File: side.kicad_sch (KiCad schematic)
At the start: 82 parts, among them J1 Conn_01x02, J2 SWD_Connector, J3 USB_C_Receptacle_USB2.0_14P, SW1 Reset Button, SW10 SW_Push, SW11 SW_Push, SW12 SW_Push, SW13 SW_Push, SW14 SW_Push, SW15 SW_Push, SW16 SW_Push, SW17 SW_Push, SW18 SW_Push, SW19 SW_Push, SW2 SW_On_Off, SW20 SW_Push, SW21 SW_Push, SW22 SW_Push, SW23 SW_Push, SW3 SW_Push, SW4 SW_Push, SW5 SW_Push, SW6 SW_Push, SW7 SW_Push, SW8 SW_Push, SW9 SW_Push, U1 nRF52840, U2 USBLC6-2SC6, Y1 JYJE 2TJ432000NYFBC

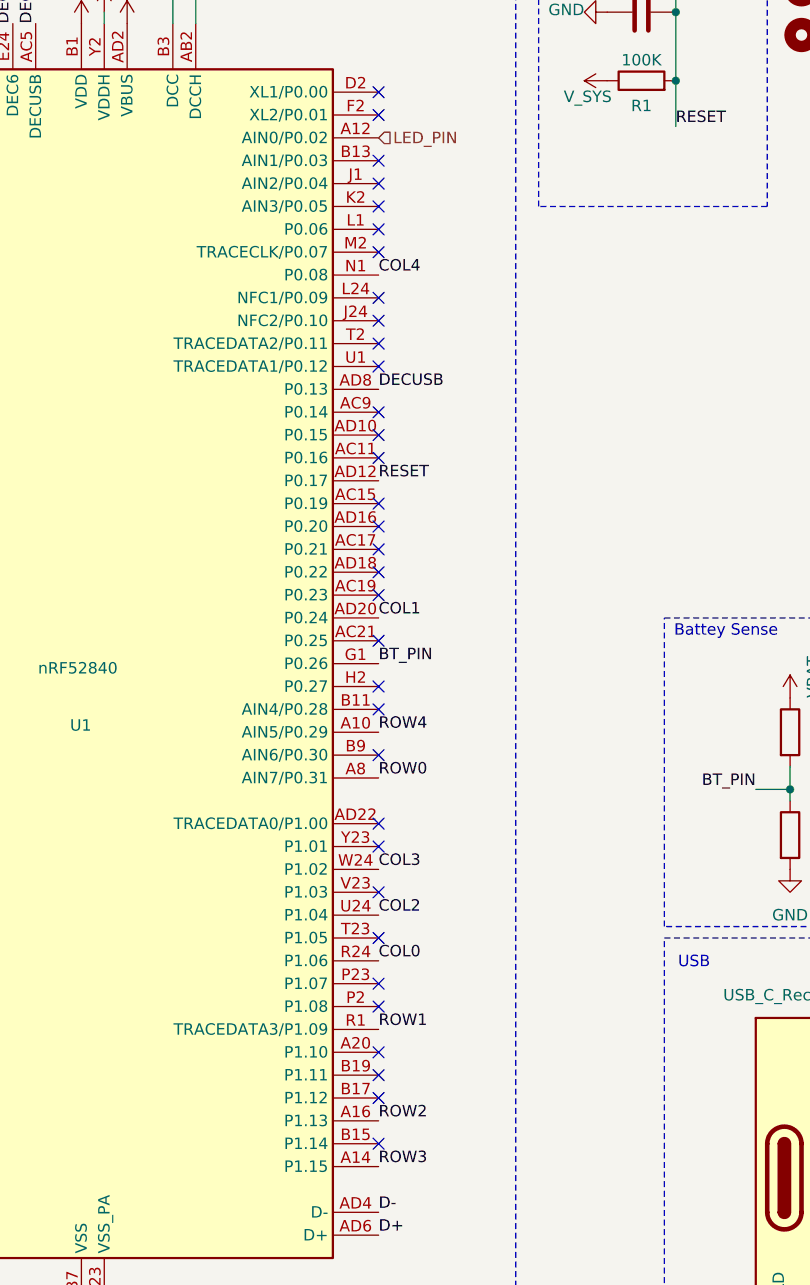
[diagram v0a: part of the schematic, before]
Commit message: routed left side
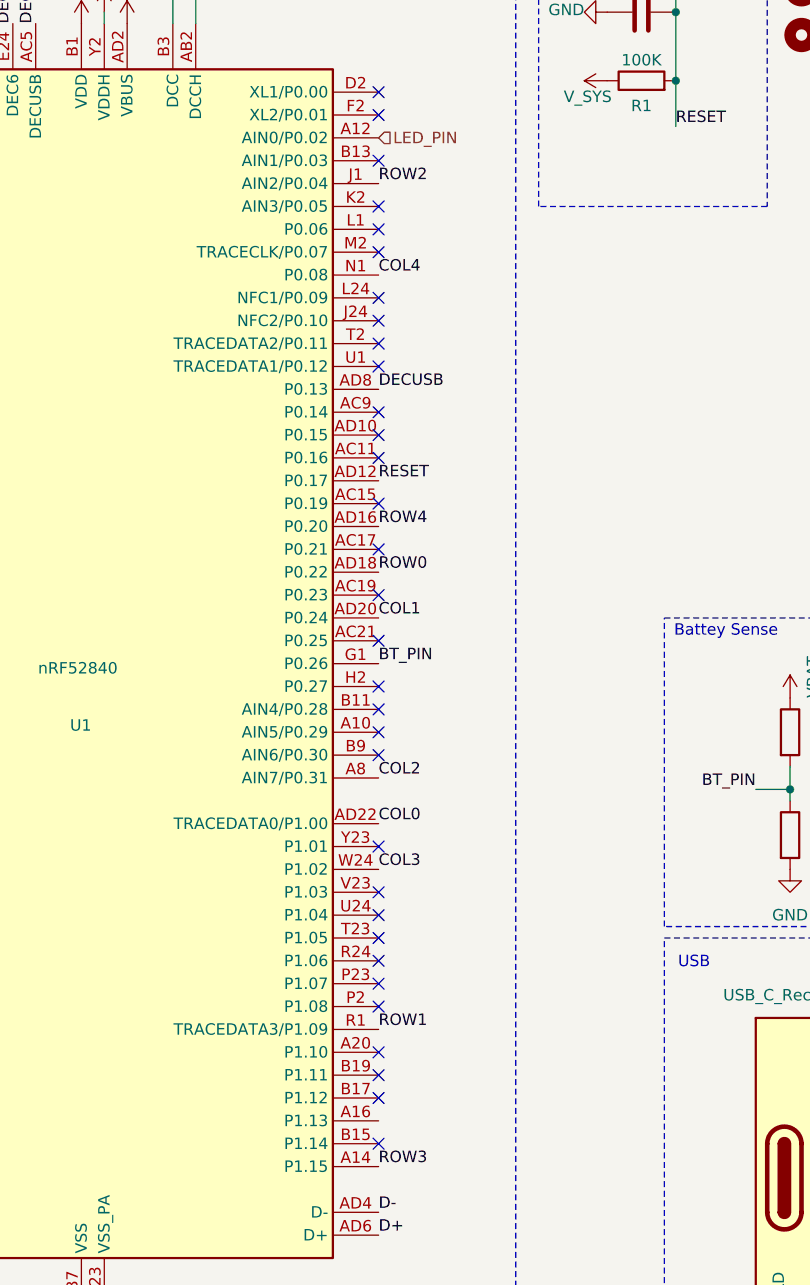
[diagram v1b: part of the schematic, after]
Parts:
- J3: footprint USB_Type_C:HRO-TYPE-C-31-M-12 -> Connector_USB:USB_C_Receptacle_XKB_U262-16XN-4BVC11; LCSC C165948 -> C963213
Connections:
- net COL0: now also U1.AD22 (TRACEDATA0/P1.00); no longer U1.R24 (P1.06)
- net COL2: now also U1.A8 (AIN7/P0.31); no longer U1.U24 (P1.04)
- net ROW0: now also U1.AD18 (P0.22); no longer U1.A8 (AIN7/P0.31)
- net ROW2: now also U1.J1 (AIN2/P0.04); no longer U1.A16 (P1.13)
- net ROW4: now also U1.AD16 (P0.20); no longer U1.A10 (AIN5/P0.29)
- no-connect marks 35 -> 34
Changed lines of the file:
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@@
 	)
 	(no_connect
+		(at 90.17 114.3)
+	)
+	(no_connect
 		(at 90.17 127)
 	)
@@
 	)
 	(no_connect
-		(at 90.17 53.34)
-	)
-	(no_connect
-		(at 90.17 91.44)
-	)
-	(no_connect
 		(at 90.17 154.94)
 	)
@@
 	)
 	(no_connect
+		(at 90.17 134.62)
+	)
+	(no_connect
 		(at 90.17 104.14)
 	)
@@
 	)
 	(no_connect
-		(at 90.17 124.46)
-	)
-	(no_connect
 		(at 90.17 111.76)
 	)
@@
 	)
 	(no_connect
-		(at 90.17 96.52)
-	)
-	(no_connect
 		(at 90.17 137.16)
 	)
@@
 		(at 90.17 78.74)
 	)
+	(no_connect
+		(at 90.17 139.7)
+	)
 	(wire
 		(pts
@@
 		)
 	)
-	(label "COL2"
-		(at 90.17 134.62 0)
+	(label "RESET"
+		(at 123.19 46.99 0)
 		(fields_autoplaced yes)
 		(effects
@@
 		)
 	)
-	(label "RESET"
-		(at 123.19 46.99 0)
+	(label "COL0"
+		(at 90.17 124.46 0)
 		(fields_autoplaced yes)
 		(effects
@@
 	)
 	(label "ROW0"
+		(at 90.17 96.52 0)
+		(fields_autoplaced yes)
+		(effects
+			(font
+				(size 1.27 1.27)
+			)
+			(justify left bottom)
+		)
+	)
+	(label "ROW0"
 		(at 158.75 74.93 180)
 		(fields_autoplaced yes)
@@
 		)
 	)
-	(label "ROW2"
-		(at 90.17 157.48 0)
-		(fields_autoplaced yes)
-		(effects
-			(font
-				(size 1.27 1.27)
-			)
-			(justify left bottom)
-		)
-	)
 	(label "DEC6"
 		(at 49.53 35.56 90)
@@
 		)
 	)
-	(label "ROW0"
-		(at 90.17 119.38 0)
-		(fields_autoplaced yes)
-		(effects
-			(font
-				(size 1.27 1.27)
-			)
-			(justify left bottom)
-		)
-	)
-	(label "COL0"
-		(at 90.17 139.7 0)
-		(fields_autoplaced yes)
-		(effects
-			(font
-				(size 1.27 1.27)
-			)
-			(justify left bottom)
-		)
-	)
 	(label "D+"
 		(at 160.02 167.64 0)
@@
 	)
 	(label "ROW4"
-		(at 90.17 114.3 0)
+		(at 90.17 91.44 0)
 		(fields_autoplaced yes)
 		(effects
@@
 		)
 	)
+	(label "COL2"
+		(at 90.17 119.38 0)
+		(fields_autoplaced yes)
+		(effects
+			(font
+				(size 1.27 1.27)
+			)
+			(justify left bottom)
+		)
+	)
 	(label "ANT"
 		(at 243.84 154.94 180)
@@
 		)
 	)
+	(label "ROW2"
+		(at 90.17 53.34 0)
+		(fields_autoplaced yes)
+		(effects
+			(font
+				(size 1.27 1.27)
+			)
+			(justify left bottom)
+		)
+	)
 	(label "XC1"
 		(at 24.13 101.6 180)
@@
 			)
 		)
-		(property "Footprint" "USB_Type_C:HRO-TYPE-C-31-M-12"
+		(property "Footprint" "Connector_USB:USB_C_Receptacle_XKB_U262-16XN-4BVC11"
 			(at 146.05 163.83 0)
 			(effects
@@
 			)
 		)
-		(property "LCSC" "C165948"
+		(property "LCSC" "C963213"
 			(at 142.24 163.83 0)
 			(effects

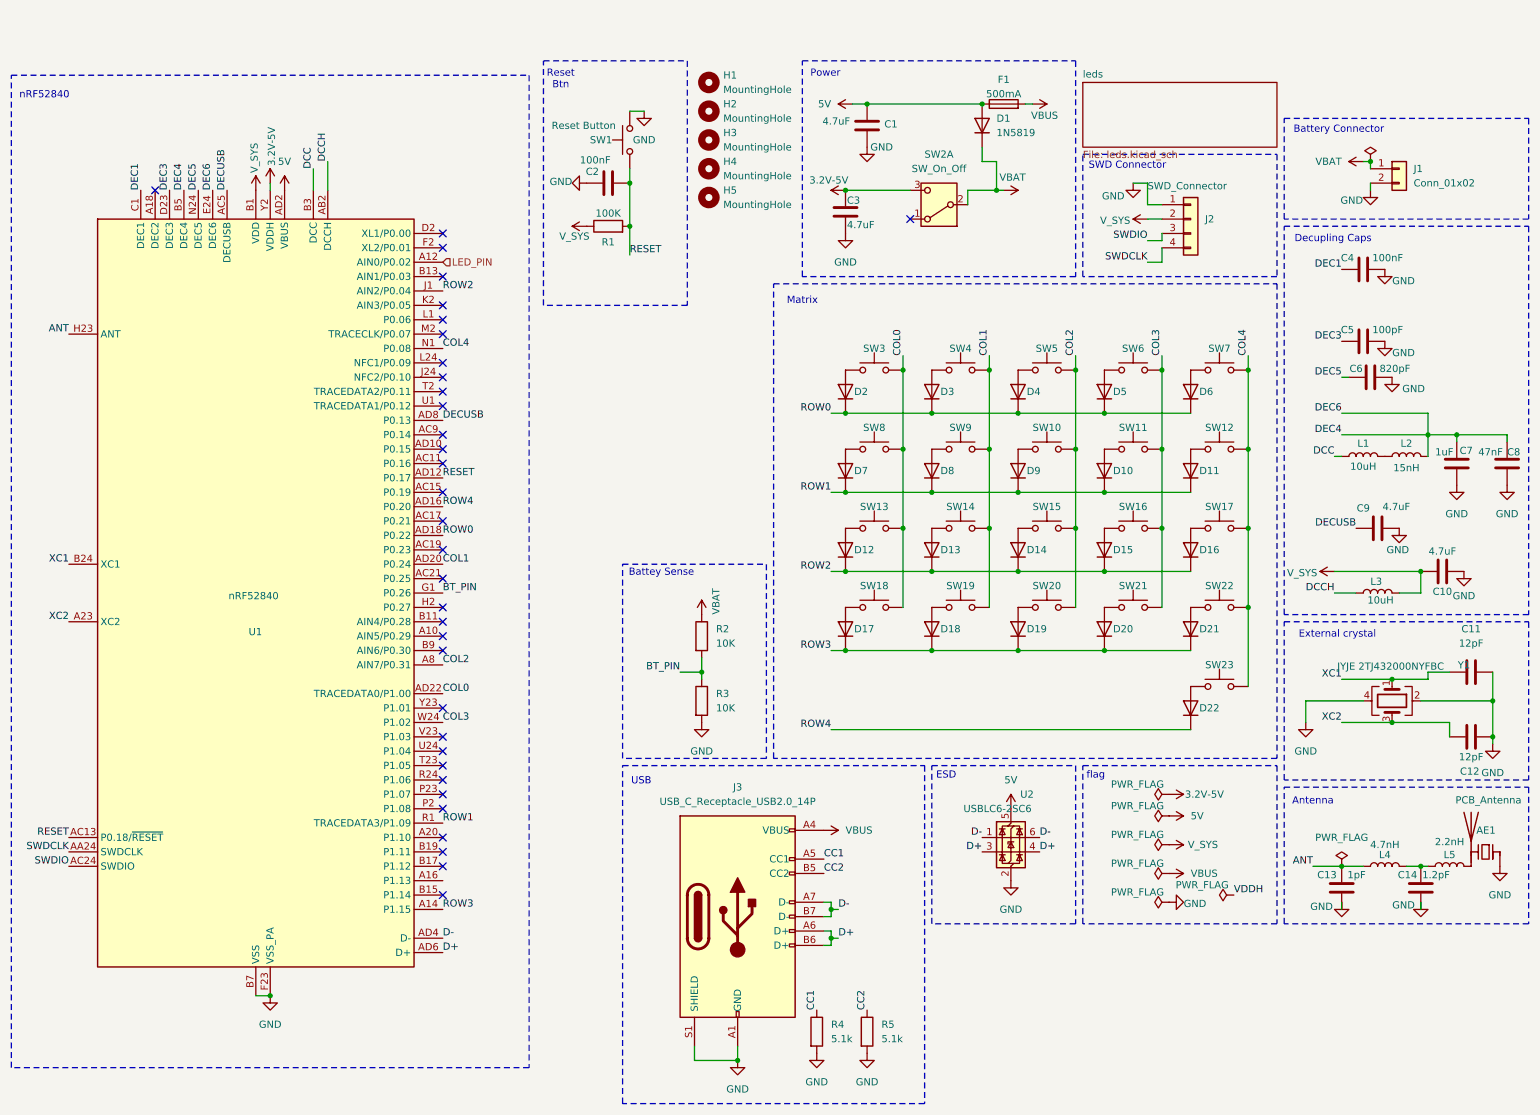
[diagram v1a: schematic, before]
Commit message: placed right side
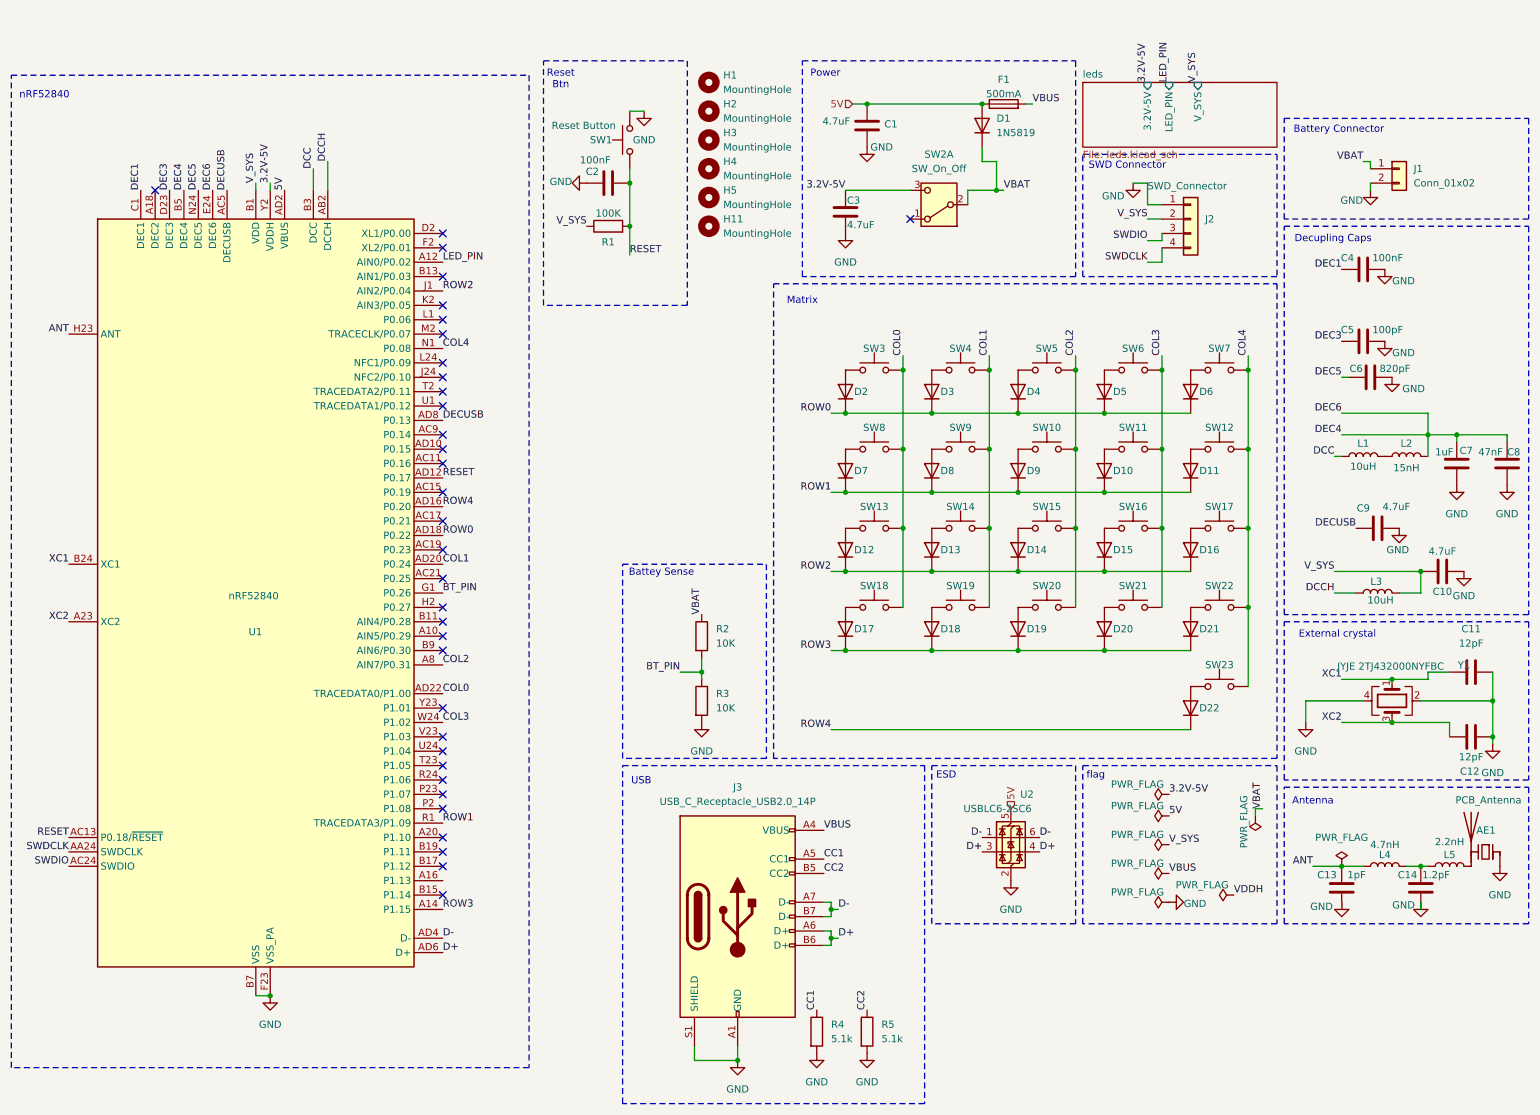
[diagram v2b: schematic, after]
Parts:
- added H11: MountingHole, MountingHole:MountingHole_2mm, symbol Mechanical:MountingHole
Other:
- sheet leds ports: added 3.2V-5V, LED_PIN, V_SYS; removed none

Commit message: added propper brake offs
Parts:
- J3: footprint Connector_USB:USB_C_Receptacle_XKB_U262-16XN-4BVC11 -> Connector_USB:USB_C_Receptacle_G-Switch_GT-USB-7025
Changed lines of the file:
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@@
 			)
 		)
-		(property "Footprint" "Connector_USB:USB_C_Receptacle_XKB_U262-16XN-4BVC11"
+		(property "Footprint" "Connector_USB:USB_C_Receptacle_G-Switch_GT-USB-7025"
 			(at 146.05 163.83 0)
 			(effects
